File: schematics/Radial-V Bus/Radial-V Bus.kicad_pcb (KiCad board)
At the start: 2 copper layers, 13 parts, among them J1 Conn_Alim, J2 Conn_Reset

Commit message: Update Bus Board
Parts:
- moved ARD-C1 10.2 mm to (134.6, 45.7)
- moved MP3-C1 10.2 mm to (116.8, 38.1)
- moved J1 7.62 mm to (43.2, 40.6)
- moved ARD-C7 6.35 mm to (120.7, 94.0)
- moved MP3-C4 6.35 mm to (120.7, 86.4)
- moved ARD-C2 5.08 mm to (111.8, 45.7)
- moved J2 3.81 mm to (82.5, 35.6), turned to 0 degrees
- moved ARD-C6 2.54 mm to (99.1, 94.0)
- moved MP3-C3 2.54 mm to (99.1, 86.4)
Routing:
- net /GND: track 0.00 -> 108.2 mm, vias 0 -> 3
- net /5V: track 66.6 -> 163.6 mm, vias 1 -> 4
- net /D51-MOSI: track 18.8 -> 81.6 mm, vias 0 -> 1
- net /D50-MISO: track 25.7 -> 81.6 mm, vias 0 -> 1
- net /RESET: track 0.00 -> 50.9 mm
- net /3V3: track 83.0 -> 121.0 mm, vias 1 -> 2
- net /GND-ARD: track 19.6 -> 34.1 mm, vias 1 -> 0
- net /D52-SCLK: track 74.3 -> 85.1 mm, vias 0 -> 1
- net Net-(ARD-C7-Pad2): track 0.00 -> 7.62 mm, vias 0 -> 1
- net Net-(ARD-C7-Pad1): track 0.00 -> 7.62 mm, vias 0 -> 1
- net /MP3-DREQ: track 0.00 -> 7.62 mm, vias 0 -> 1
- net /MP3-DCS: track 0.00 -> 7.62 mm, vias 0 -> 1
- net /MP3-CS: track 0.00 -> 7.62 mm, vias 0 -> 1
- net /GPIO1: track 0.00 -> 7.62 mm, vias 0 -> 1
- net /A12: track 104.4 -> 112.1 mm
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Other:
- board outline added: 118.1 x 77.5 mm
- net class Alimentation added: clearance 0.2, trace_width 0.25, via_dia 0.8, via_drill 0.4
- board text added: "5v"
- board text added: "A0"
- board text added: "A15"
- board text added: "A7"
- board text added: "A8"
- board text added: "ALIM (0v)"
- board text added: "ALIM (5v)"
- board text added: "Arduino Mega"
- board text added: "D0"
- board text added: "D13"
- board text added: "D14"
- board text added: "D21"
- board text added: "D23"
- board text added: "D34"
- board text added: "D7"
- board text added: "D8"
- board text added: "Distance between D7 and D8 is 150 mils (3.81mm)"
- board text added: "MP3 Player Shield"
- board text added: "POWER"
- board text added: "RADIAL-V Bus Board"
- board text added: "RESET"
- board text removed: "Bus Board"
- board text removed: "RADIAL-V"

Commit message: Routage Bus Board
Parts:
- MP3-C1, MP3-C3, MP3-C4: footprint Connector_PinHeader_2.54mm:PinHeader_1x08_P2.54mm_Vertical -> Connector_PinSocket_2.54mm:PinSocket_1x08_P2.54mm_Vertical
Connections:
- ARD-C4 pad 30: Net-(ARD-C4-Pad30) -> /D49
- PL1 pad 23: /D52-SCLK -> /D49
- PL1 pad 25: /D51-MOSI -> /GND-ARD
- PL1 pad 26: /D50-MISO -> /5V
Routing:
- net /D29: track 22.4 -> 82.7 mm, vias 0 -> 2
- net /D3: track 148.7 -> 90.2 mm, vias 0 -> 2
- net /D41: track 22.4 -> 76.7 mm, vias 0 -> 2
- net /D37: track 21.4 -> 74.4 mm, vias 0 -> 2
- net /D33: track 21.4 -> 72.1 mm, vias 0 -> 2
- net /D25: track 23.5 -> 72.8 mm, vias 0 -> 2
- net /D19: track 114.3 -> 69.9 mm, vias 0 -> 2
- net /D47: track 21.4 -> 63.1 mm, vias 0 -> 2
- net /5V: track 163.6 -> 195.8 mm
- net /SCL: track 69.9 -> 42.7 mm, vias 0 -> 2
- net /D51-MOSI: track 81.6 -> 103.6 mm, vias 1 -> 3
- net /D49: track 0.00 -> 18.8 mm
- net /GND-ARD: track 34.1 -> 49.6 mm
- net /A12: track 112.1 -> 115.8 mm
- net /D17: track 94.3 -> 97.7 mm
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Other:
- board size 118.1 x 77.5 mm -> 118.1 x 76.2 mm
- net class Alimentation removed
- net class Default: clearance 0.2 -> 0.5; trace_width 0.25 -> 0.3
- net class Power added: clearance 0.5, trace_width 0.5, via_dia 0.8, via_drill 0.4
- rule trace_clearance: 0.2 -> 0.5

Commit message: Bus Board
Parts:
- J2: footprint Connector_Molex:Molex_KK-254_AE-6410-02A_1x02_P2.54mm_Vertical -> Connector_JST:JST_EH_B2B-EH-A_1x02_P2.50mm_Vertical
- moved J2 5.68 mm to (87.6, 38.1), turned to 180 degrees
- moved J1 2.62 mm to (43.8, 38.1), turned to 270 degrees
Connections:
- ARD-C4 pad 18: /D37 -> Net-(ARD-C4-Pad18)
- J1 pad 1: /GND-ARD -> /5V
- J1 pad 2: /5V -> /GND-ARD
- PL1 pad 14: /D37 -> /RESET
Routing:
- net /RESET: track 50.9 -> 157.9 mm, vias 0 -> 2
- net /D37: track 74.4 -> 0.00 mm, vias 2 -> 0
- net /A12: track 115.8 -> 107.0 mm
- net /A14: track 99.3 -> 91.8 mm
- net /GND: track 108.2 -> 102.1 mm, vias 3 -> 4
- net /D41: track 76.7 -> 78.5 mm
- net /GND-ARD: track 49.6 -> 48.9 mm, vias 0 -> 1
- net /5V: vias 4 -> 6
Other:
- board size 118.1 x 76.2 mm -> 115.6 x 76.2 mm
- board text added: "D18"
- board text added: "D25"
- board text added: "D27"
- board text added: "D29"
- board text added: "D3"
- board text added: "D31"
- board text added: "D33"
- board text added: "D35"
- board text added: "D39"
- board text added: "D41"
- board text added: "D43"
- board text added: "D45"
- board text added: "D47"
- board text added: "D49"
- board text added: "GND"
- board text added: "MISO"
- board text added: "MOSI"
- board text added: "SCLK"
- board text added: "X"
- board text removed: "D34"

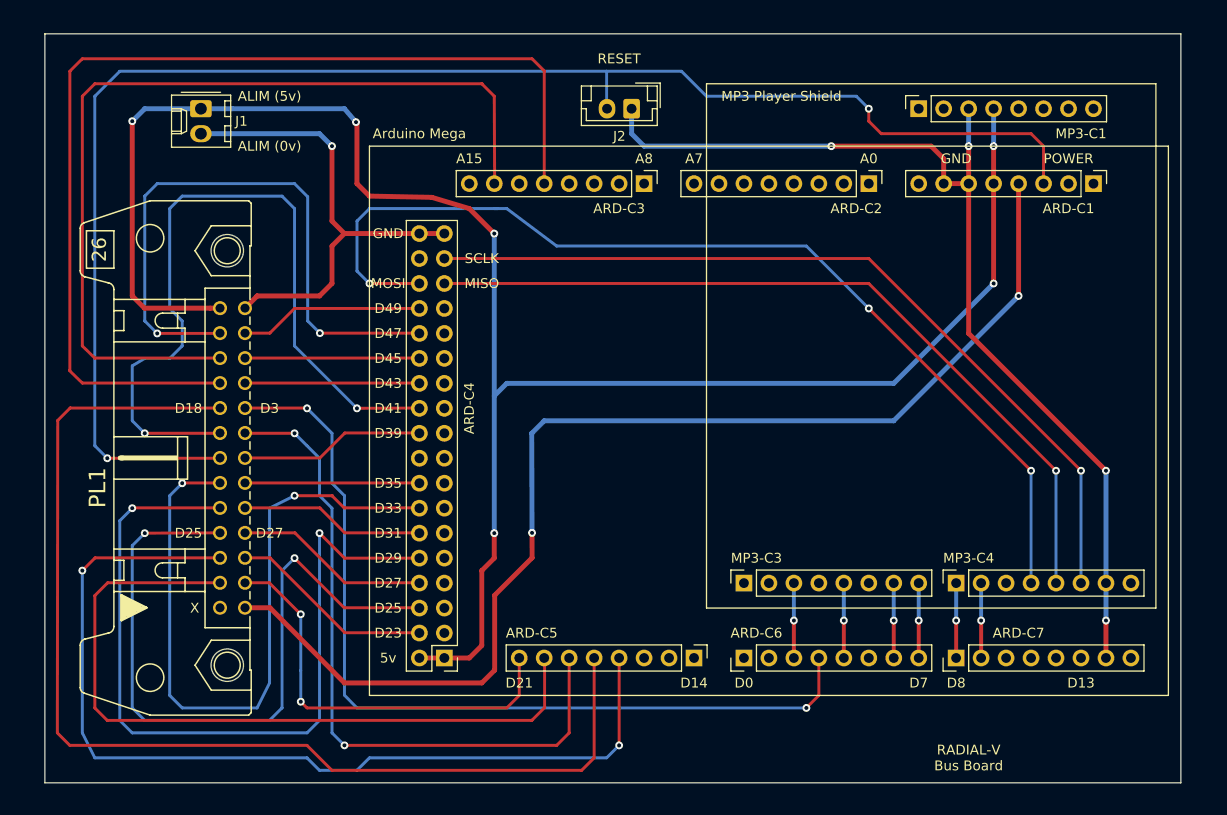
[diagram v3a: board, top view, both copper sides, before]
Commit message: Ajout de Radio Board
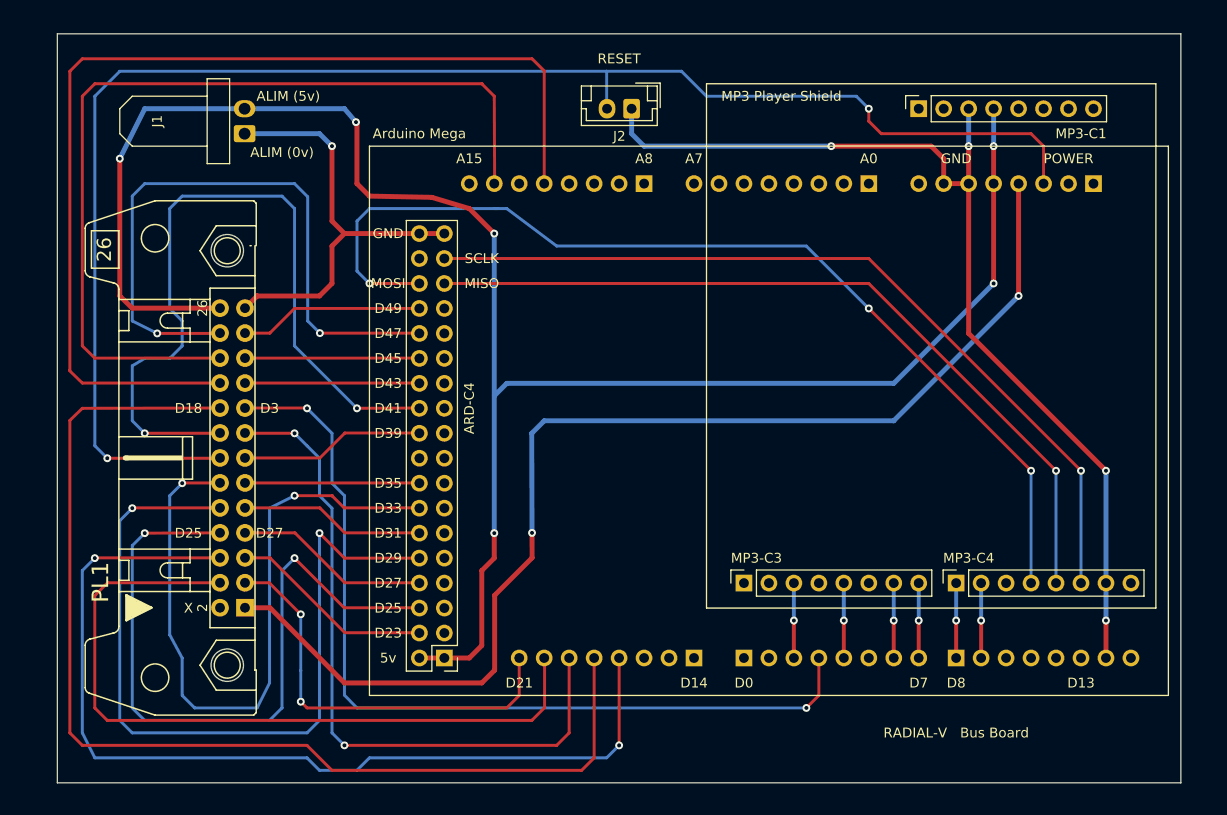
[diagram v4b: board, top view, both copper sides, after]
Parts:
- ARD-C1, ARD-C2, ARD-C3, ARD-C5, ARD-C6, ARD-C7: moved to B.Cu
- J1: footprint Connector_Molex:Molex_KK-254_AE-6410-02A_1x02_P2.54mm_Vertical -> MesModules:Molex_KK-254_AE-6410-02A_1x02_P2.54mm_Horizontal
- PL1: value vers Ext. Board -> Nappe; footprint Radial-V Bus:26H -> MesModules:HE10-26P
- moved J1 5.12 mm to (48.3, 40.6), turned to 90 degrees
- turned ARD-C1 to 90 degrees
- turned ARD-C2 to 90 degrees
- turned ARD-C3 to 90 degrees
- turned ARD-C5 to 90 degrees
- turned ARD-C6 to 270 degrees
- turned ARD-C7 to 270 degrees
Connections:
- net /RESET renamed RESET
- J1 pad 1: /5V -> /GND-ARD
- J1 pad 2: /GND-ARD -> /5V
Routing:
- net /GND-ARD: track 48.9 -> 44.5 mm
- net /D18: track 115.7 -> 113.2 mm
- net /D47: track 63.1 -> 65.4 mm
- net /5V: track 195.8 -> 197.1 mm
- net /D33: track 72.1 -> 71.2 mm
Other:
- board size 115.6 x 76.2 mm -> 114.3 x 76.2 mm

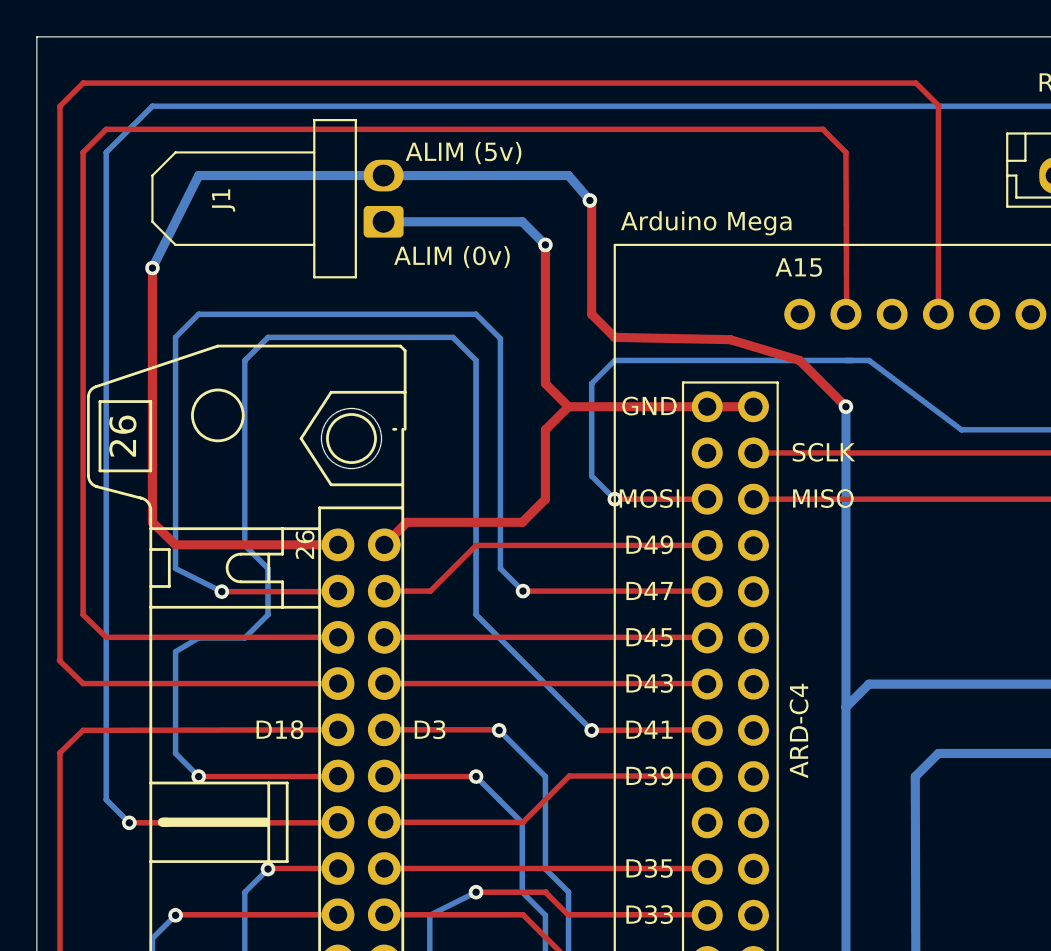
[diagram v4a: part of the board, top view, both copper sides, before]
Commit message: Regroupement de A12 et A14 sur le même connecteur
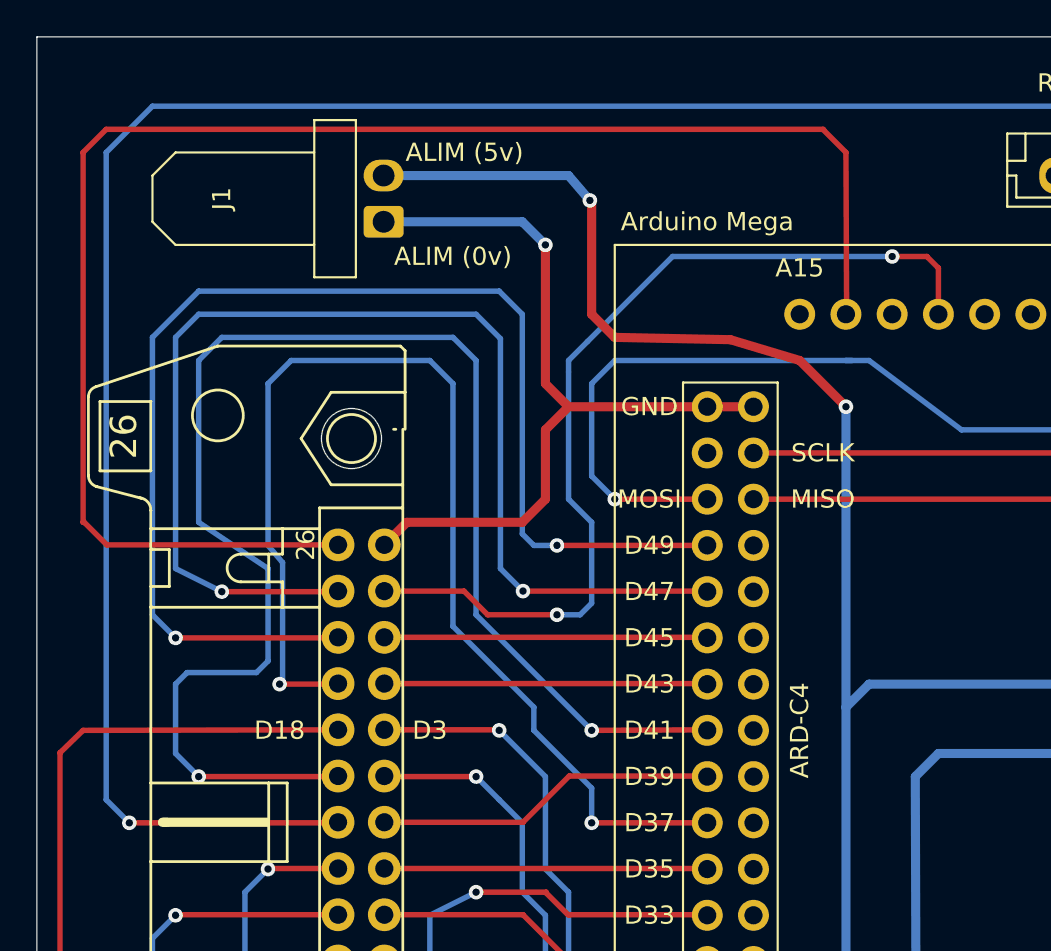
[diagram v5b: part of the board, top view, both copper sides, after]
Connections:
- ARD-C4 pad 18: Net-(ARD-C4-Pad18) -> /D37
- PL1 pad 20: /A12 -> /D37
- PL1 pad 22: /A14 -> /D49
- PL1 pad 23: /D49 -> /A12
- PL1 pad 26: /5V -> /A14
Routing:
- net /D37: track 0.00 -> 64.9 mm, vias 0 -> 2
- net /A12: track 107.0 -> 51.5 mm, vias 0 -> 2
- net /D49: track 18.8 -> 70.4 mm, vias 0 -> 2
- net /5V: track 197.1 -> 156.6 mm, vias 6 -> 5
- net /A14: track 91.8 -> 86.7 mm
- net /D41: track 78.5 -> 83.1 mm
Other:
- board text added: "D37"

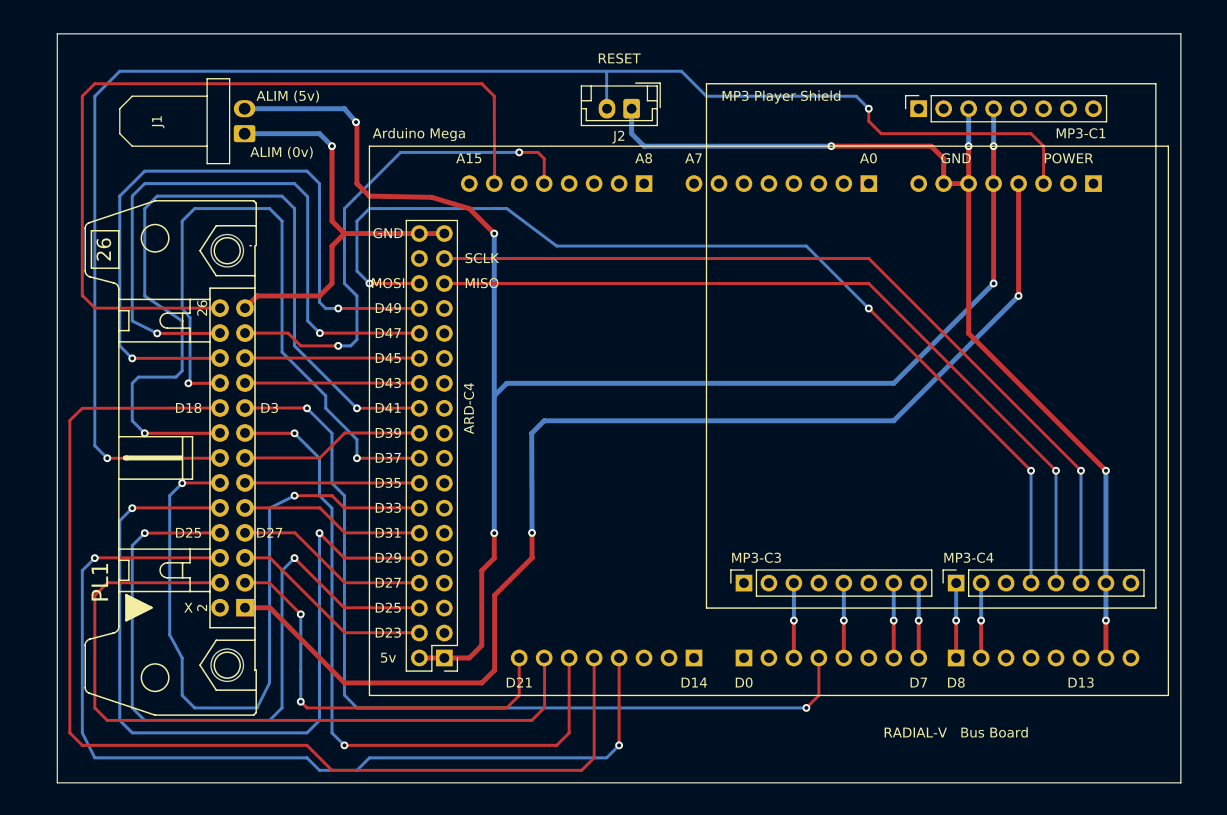
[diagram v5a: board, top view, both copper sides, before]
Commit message: Header ARD-J4 mis sur la couche Bottom
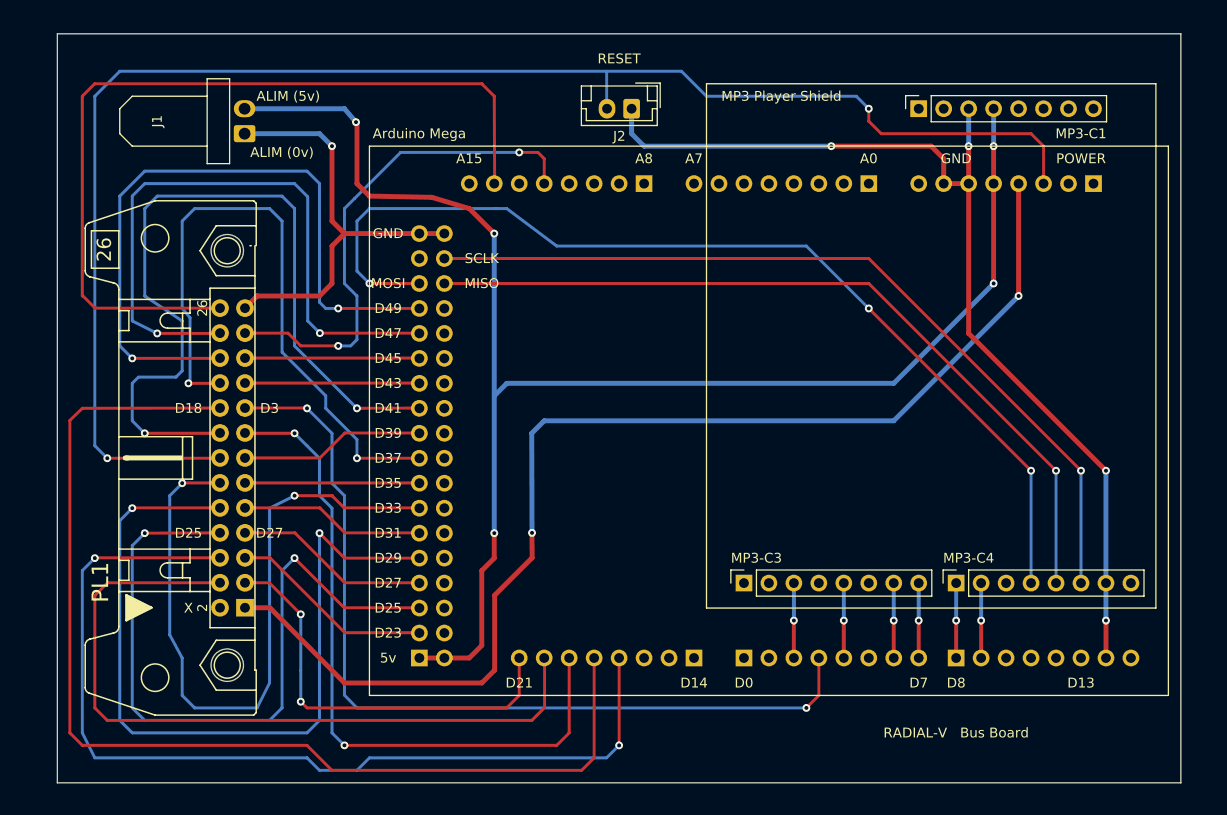
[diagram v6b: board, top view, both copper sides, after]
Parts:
- ARD-C4: moved to B.Cu
- moved ARD-C4 2.54 mm to (66.0, 94.0), turned to 0 degrees
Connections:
- ARD-C4 pad 10: /D29 -> Net-(ARD-C4-Pad10)
- ARD-C4 pad 11: Net-(ARD-C4-Pad11) -> /D31
- ARD-C4 pad 12: /D31 -> Net-(ARD-C4-Pad12)
- ARD-C4 pad 13: Net-(ARD-C4-Pad13) -> /D33
- ARD-C4 pad 14: /D33 -> Net-(ARD-C4-Pad14)
- ARD-C4 pad 15: Net-(ARD-C4-Pad15) -> /D35
- ARD-C4 pad 16: /D35 -> Net-(ARD-C4-Pad16)
- ARD-C4 pad 17: Net-(ARD-C4-Pad17) -> /D37
- ARD-C4 pad 18: /D37 -> Net-(ARD-C4-Pad18)
- ARD-C4 pad 19: Net-(ARD-C4-Pad19) -> /D39
- ARD-C4 pad 20: /D39 -> Net-(ARD-C4-Pad20)
- ARD-C4 pad 21: Net-(ARD-C4-Pad21) -> /D41
- ARD-C4 pad 22: /D41 -> Net-(ARD-C4-Pad22)
- ARD-C4 pad 23: Net-(ARD-C4-Pad23) -> /D43
- ARD-C4 pad 24: /D43 -> Net-(ARD-C4-Pad24)
- ARD-C4 pad 25: Net-(ARD-C4-Pad25) -> /D45
- ARD-C4 pad 26: /D45 -> Net-(ARD-C4-Pad26)
- ARD-C4 pad 27: Net-(ARD-C4-Pad27) -> /D47
- ARD-C4 pad 28: /D47 -> Net-(ARD-C4-Pad28)
- ARD-C4 pad 29: Net-(ARD-C4-Pad29) -> /D49
- ARD-C4 pad 3: Net-(ARD-C4-Pad3) -> /D23
- ARD-C4 pad 30: /D49 -> Net-(ARD-C4-Pad30)
- ARD-C4 pad 31: /D50-MISO -> /D51-MOSI
- ARD-C4 pad 32: /D51-MOSI -> /D50-MISO
- ARD-C4 pad 33: /D52-SCLK -> Net-(ARD-C4-Pad33)
- ARD-C4 pad 34: Net-(ARD-C4-Pad34) -> /D52-SCLK
- ARD-C4 pad 4: /D23 -> Net-(ARD-C4-Pad4)
- ARD-C4 pad 5: Net-(ARD-C4-Pad5) -> /D25
- ARD-C4 pad 6: /D25 -> Net-(ARD-C4-Pad6)
- ARD-C4 pad 7: Net-(ARD-C4-Pad7) -> /D27
- ARD-C4 pad 8: /D27 -> Net-(ARD-C4-Pad8)
- ARD-C4 pad 9: Net-(ARD-C4-Pad9) -> /D29
